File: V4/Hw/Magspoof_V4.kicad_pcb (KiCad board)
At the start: 2 copper layers, 39.5 x 21.9 mm, 47 parts, among them J1 Coil, J2 SWD, P1 USB_C_Plug_USB2.0, Q1 DMG3415U-7, SW1 ON, SW3 S1, SW4 SOURCE MAG, SW5 RESET, U1 CH552G, U2 AP2112K-3.3, U3 TC4424, U5 MCP73831

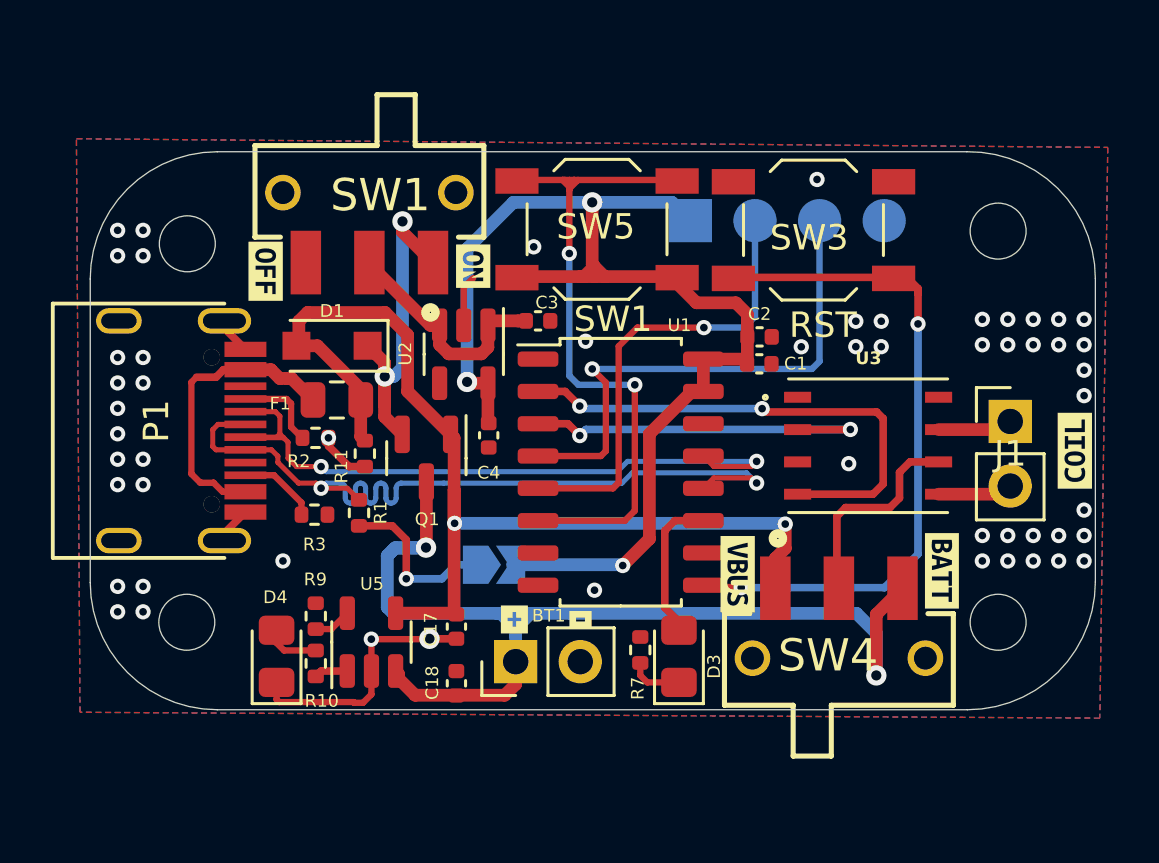
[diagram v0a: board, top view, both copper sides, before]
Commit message: change footprint of SW1,4, and F1 and routing
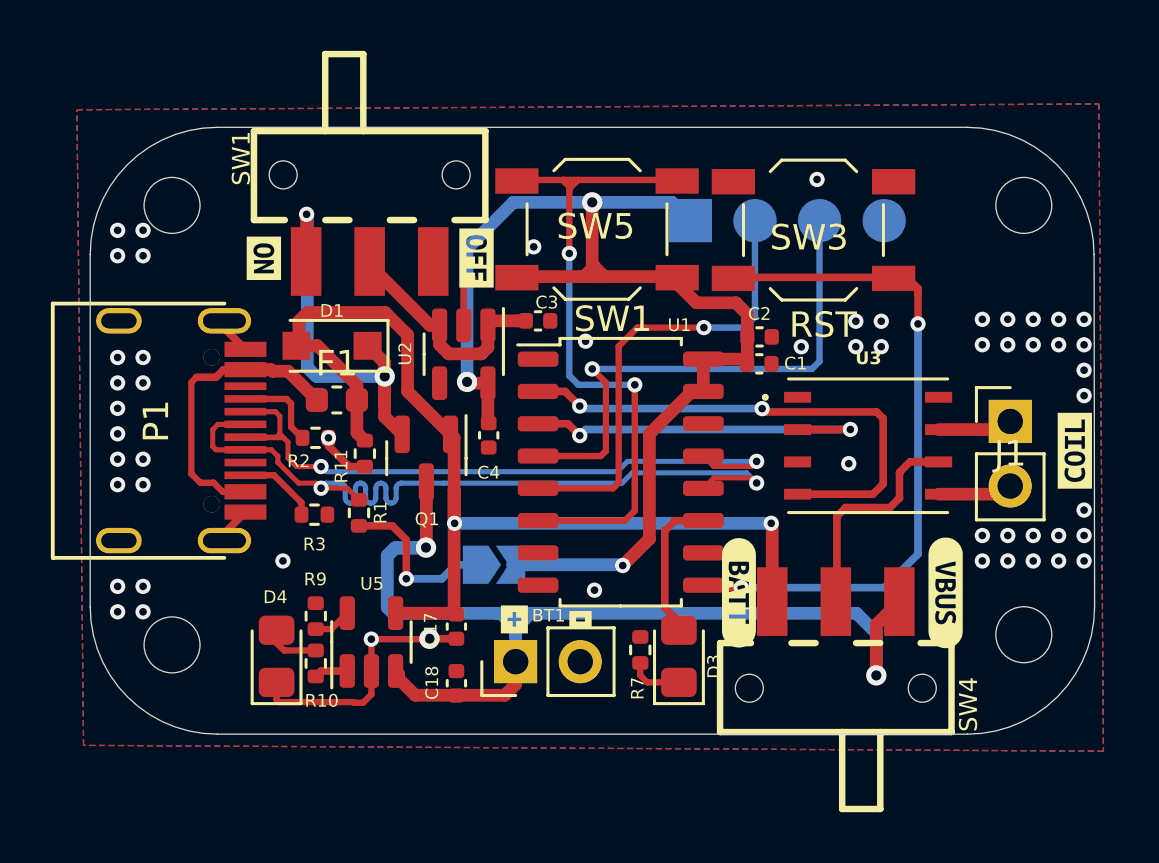
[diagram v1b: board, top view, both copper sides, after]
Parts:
- removed kibuzzard-6436F03D: G***, kibuzzard-6436F03D
- removed kibuzzard-6436F054: G***, kibuzzard-6436F054
- added kibuzzard-64629FC5: G***, kibuzzard-64629FC5, F.Cu at (130.6, 63.8)
- added kibuzzard-64629FDC: G***, kibuzzard-64629FDC, F.Cu at (122.4, 63.8)
- F1: footprint Fuse:Fuse_0805_2012Metric -> Fuse:Fuse_0603_1608Metric
- SW1, SW4: footprint Library:JS102011SAQN -> Library:SW-SMD_K3-1280S-K1
- moved kibuzzard-6436EF98 8.31 mm to (112.1, 50.6)
- moved kibuzzard-6436EF9F 8.24 mm to (103.8, 50.6)
- moved H1 1.62 mm to (100.1, 48.5)
- moved H2 1.43 mm to (133.6, 48.5)
- moved H4 1.12 mm to (133.6, 65.5)
- moved H3 1.06 mm to (100.1, 65.8)
- moved SW1 0.96 mm to (107.9, 50.7), turned to 90 degrees
- moved SW4 0.49 mm to (126.2, 64.1), turned to -90 degrees
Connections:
- SW4 pad 1: VBUS -> +BATT
- SW4 pad 3: +BATT -> VBUS
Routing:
- net Net-(D1-K): track 14.1 -> 16.3 mm
- net Net-(F1-Pad1): track 12.6 -> 11.6 mm
- net +BATT: track 43.3 -> 42.7 mm
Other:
- board size 39.5 x 21.9 mm -> 39.5 x 23.9 mm

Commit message: change SW1 and SW4 for stocks
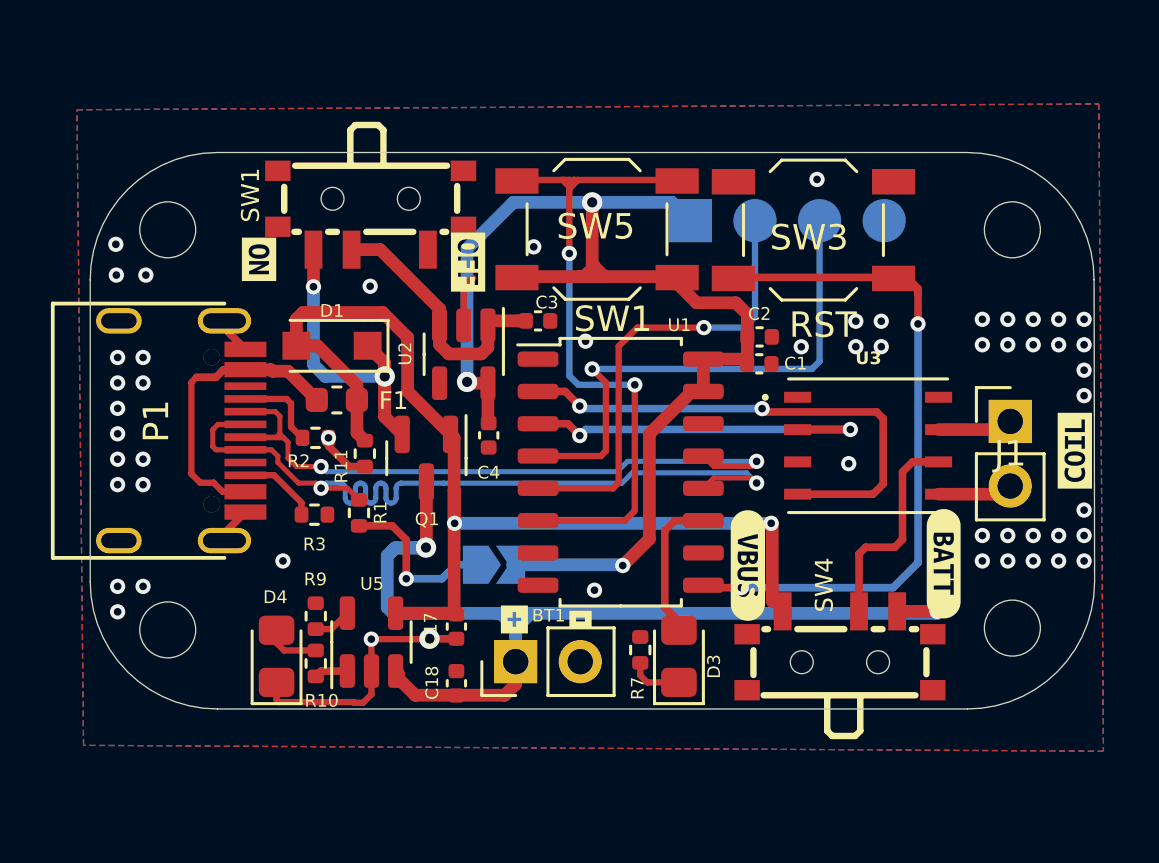
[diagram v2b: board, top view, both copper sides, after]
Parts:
- SW1, SW4: footprint Library:SW-SMD_K3-1280S-K1 -> Library:SW-SMD_SSSS811101
- moved kibuzzard-64629FDC 8.13 mm to (130.5, 62.6)
- moved kibuzzard-64629FC5 7.85 mm to (122.8, 62.7)
- moved SW1 2.02 mm to (108.0, 48.7), turned to 180 degrees
- moved SW4 1.94 mm to (126.4, 66.0), turned to 0 degrees
- moved H2 1.06 mm to (133.2, 49.5)
- moved H1 0.97 mm to (100.0, 49.5)
- moved H3 0.61 mm to (100.0, 65.2)
- moved H4 0.52 mm to (133.2, 65.2)
- moved kibuzzard-6436EF98 0.37 mm to (111.8, 50.8)
- moved kibuzzard-6436EF9F 0.19 mm to (103.6, 50.6)
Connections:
- SW1 pad 1: Net-(D1-K) -> (no net)
- SW1 pad 3: (no net) -> Net-(D1-K)
- SW4 pad 1: +BATT -> VBUS
- SW4 pad 3: VBUS -> +BATT
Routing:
- net Net-(D1-K): track 16.3 -> 12.7 mm
- net +BATT: track 42.7 -> 42.1 mm
- net Net-(SW1-B): track 9.62 -> 10.1 mm
- net GND: vias 55 -> 54
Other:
- board size 39.5 x 23.9 mm -> 39.5 x 21.9 mm

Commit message: Update labels
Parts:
- added REF**: OSHW-Logo_5.7x6mm_SilkScreen, Symbol:OSHW-Logo_5.7x6mm_SilkScreen, B.Cu at (106.2, 57.4)
- added kibuzzard-64665C6A: G***, kibuzzard-64665C6A, F.Cu at (102.5, 66.1)
- added kibuzzard-64665C9F: G***, kibuzzard-64665C9F, B.Cu at (108.7, 62.7)

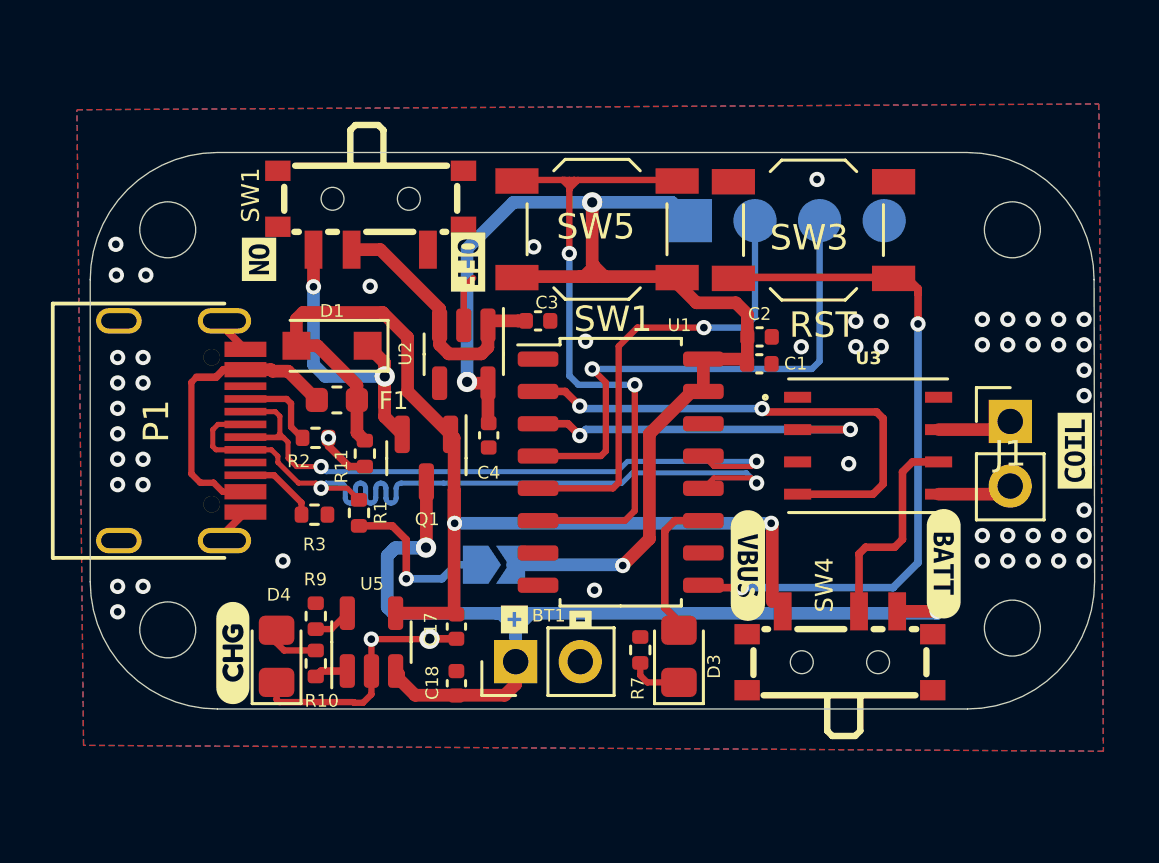
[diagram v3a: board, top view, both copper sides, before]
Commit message: change DFN-8 to SOIC-8 TC4424 and add 3d model of SW1,4
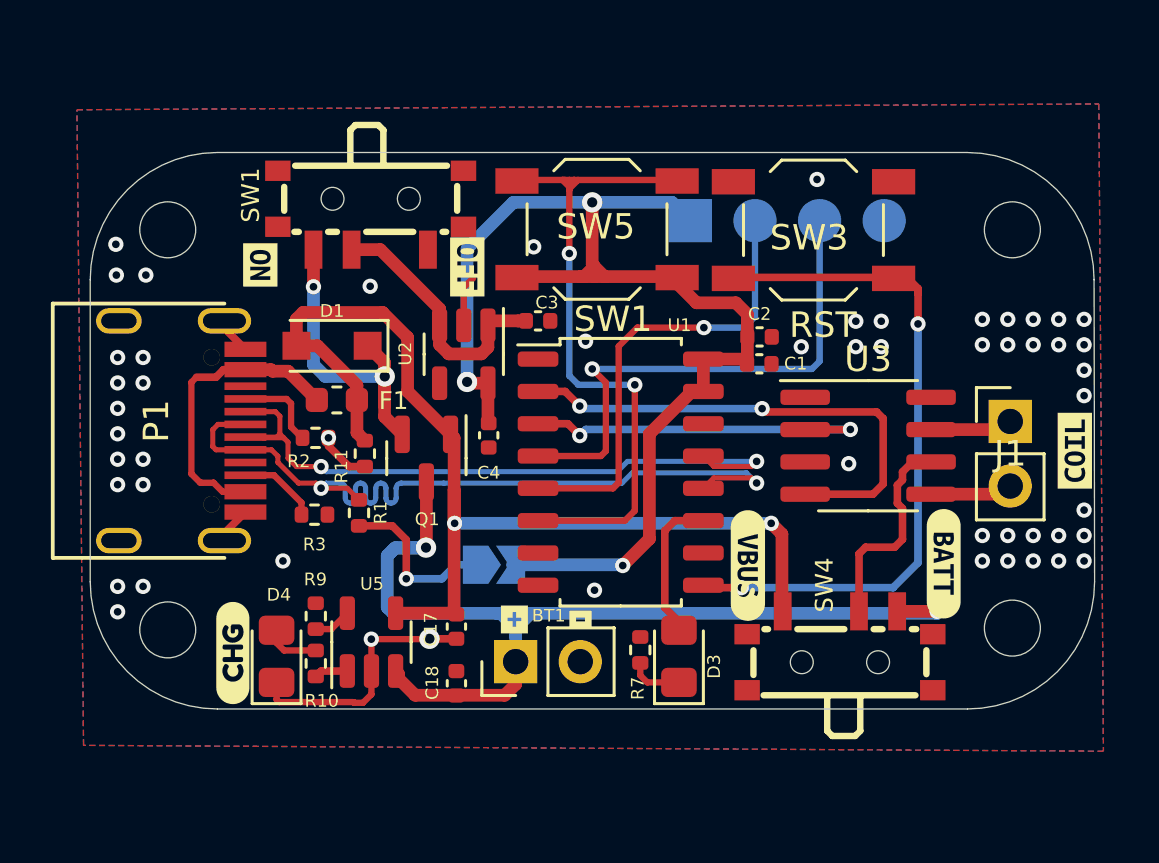
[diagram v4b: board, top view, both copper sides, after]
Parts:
- U3: footprint Library:TC4424EMF(v3) -> Package_SO:SOIC-8_3.9x4.9mm_P1.27mm
- moved kibuzzard-6436EF9F 0.23 mm to (103.6, 50.9)
- moved kibuzzard-6436EF98 0.19 mm to (111.8, 50.9)
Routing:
- net VBUS: track 42.2 -> 42.8 mm

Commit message: fix serigraphy "SW1"for "RST"
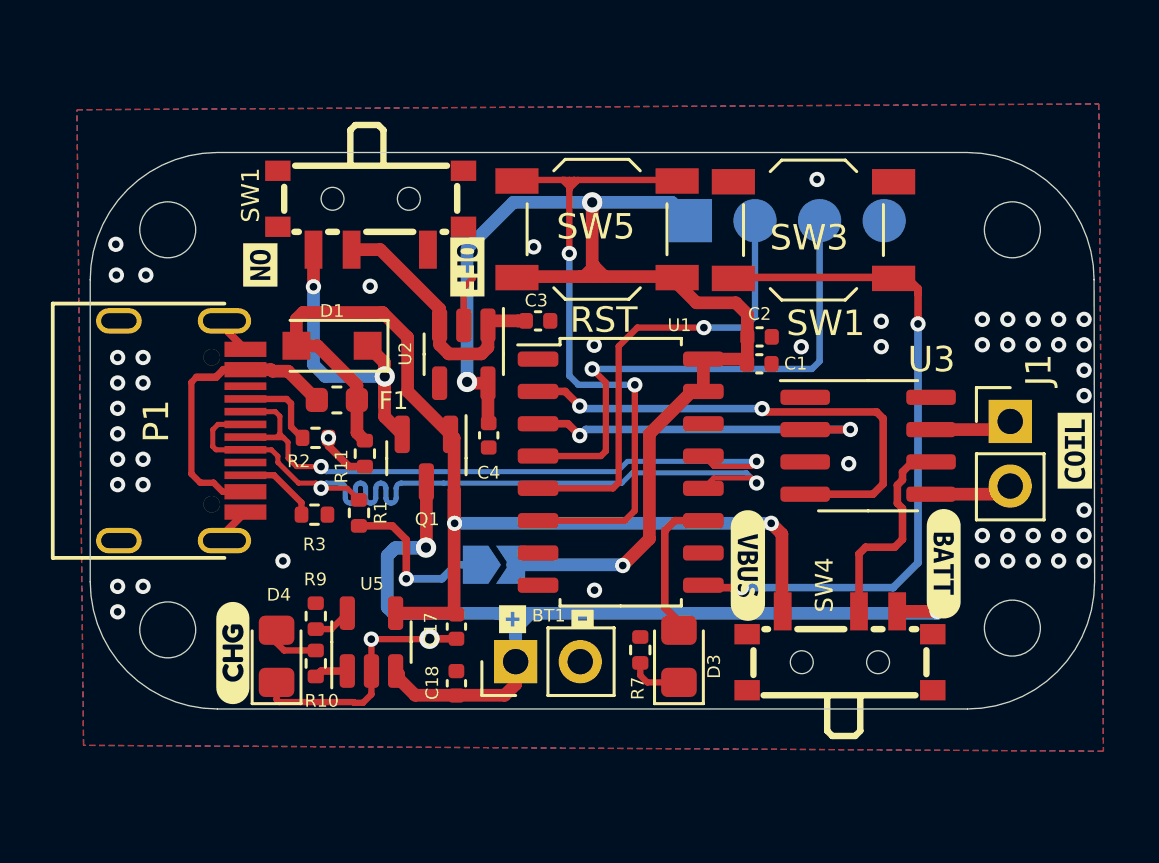
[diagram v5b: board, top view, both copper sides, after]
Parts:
- moved kibuzzard-6436EA46 0.09 mm to (116.3, 64.8)
- moved kibuzzard-6436EA37 0.07 mm to (113.5, 64.8)
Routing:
- net GND: vias 54 -> 52
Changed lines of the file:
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@@
     (property "manf#" "-")
     (attr through_hole)
-    (fp_text reference "J1" (at 0 1.27) (layer "F.SilkS")
+    (fp_text reference "J1" (at 1.124 -2.025 90) (layer "F.SilkS")
         (effects (font (size 1 1) (thickness 0.15)))
     )
@@
     (property "manf#" "TC4424AVOA713")
     (attr smd)
-    (fp_text reference "U3" (at 0 -3.4) (layer "F.SilkS")
+    (fp_text reference "U3" (at 2.492 -3.39) (layer "F.SilkS")
         (effects (font (size 1 1) (thickness 0.15)))
     )
@@
     (property "manf#" "CL05A106MP5NUNC")
     (attr smd)
-    (fp_text reference "C3" (at 0.35 -0.72 180) (layer "F.SilkS")
+    (fp_text reference "C3" (at -0.07 -0.8 180) (layer "F.SilkS")
         (effects (font (size 0.5 0.5) (thickness 0.125)))
     )
@@
   )
   (footprint "kibuzzard-6436EA46" (layer "F.Cu")
-    (at 116.2 64.8)
+    (at 116.28 64.76)
     (descr "Generated with KiBuzzard")
     (tags "kb_params=eyJBbGlnbm1lbnRDaG9pY2UiOiAiQ2VudGVyIiwgIkNhcExlZnRDaG9pY2UiOiAiWyIsICJDYXBSaWdodENob2ljZSI6ICJdIiwgIkZvbnRDb21ib0JveCI6ICJVYnVudHVNb25vLUIiLCAiSGVpZ2h0Q3RybCI6ICIuOCIsICJMYXllckNvbWJvQm94IjogIkYuU2lsa1MiLCAiTXVsdGlMaW5lVGV4dCI6ICItIiwgIlBhZGRpbmdCb3R0b21DdHJsIjogIjUiLCAiUGFkZGluZ0xlZnRDdHJsIjogIjUiLCAiUGFkZGluZ1JpZ2h0Q3RybCI6ICI1IiwgIlBhZGRpbmdUb3BDdHJsIjogIjUiLCAiV2lkdGhDdHJsIjogIiJ9")
@@
   )
   (footprint "kibuzzard-6436EA37" (layer "F.Cu")
-    (at 113.6 64.8)
+    (at 113.53 64.79)
     (descr "Generated with KiBuzzard")
     (tags "kb_params=eyJBbGlnbm1lbnRDaG9pY2UiOiAiQ2VudGVyIiwgIkNhcExlZnRDaG9pY2UiOiAiWyIsICJDYXBSaWdodENob2ljZSI6ICJdIiwgIkZvbnRDb21ib0JveCI6ICJVYnVudHVNb25vLUIiLCAiSGVpZ2h0Q3RybCI6ICIuOCIsICJMYXllckNvbWJvQm94IjogIkYuU2lsa1MiLCAiTXVsdGlMaW5lVGV4dCI6ICIrIiwgIlBhZGRpbmdCb3R0b21DdHJsIjogIjUiLCAiUGFkZGluZ0xlZnRDdHJsIjogIjUiLCAiUGFkZGluZ1JpZ2h0Q3RybCI6ICI1IiwgIlBhZGRpbmdUb3BDdHJsIjogIjUiLCAiV2lkdGhDdHJsIjogIiJ9")
@@
     (effects (font (size 1 1) (thickness 0.15)) (justify mirror))
   )
-  (gr_text "SW1" (at 115.93 53.58) (layer "F.SilkS")
+  (gr_text "SW1" (at 124.29 53.74) (layer "F.SilkS")
     (effects (font (size 1 1) (thickness 0.15)) (justify left bottom))
   )
-  (gr_text "RST" (at 124.4 53.81) (layer "F.SilkS")
+  (gr_text "RST" (at 115.78 53.61) (layer "F.SilkS")
     (effects (font (size 1 1) (thickness 0.15)) (justify left bottom))
   )
@@
   (via (at 128.025 54.075) (size 0.6) (drill 0.3) (layers "F.Cu" "B.Cu") (free) (net 2))
   (via (at 107.975 65.575) (size 0.6) (drill 0.3) (layers "F.Cu" "B.Cu") (net 2))
-  (via (at 116.4 53.86) (size 0.6) (drill 0.3) (layers "F.Cu" "B.Cu") (free) (net 2))
+  (via (at 116.74 54.02) (size 0.6) (drill 0.3) (layers "F.Cu" "B.Cu") (free) (net 2))
   (via (at 107.93 51.7) (size 0.6) (drill 0.3) (layers "F.Cu" "B.Cu") (free) (net 2))
   (via (at 126.746 58.674) (size 0.6) (drill 0.3) (layers "F.Cu" "B.Cu") (free) (net 2))
@@
   (via (at 110.26 65.56) (size 0.8) (drill 0.4) (layers "F.Cu" "B.Cu") (net 2))
   (via (at 132 61.5) (size 0.6) (drill 0.3) (layers "F.Cu" "B.Cu") (free) (net 2))
-  (via (at 127.025 54.075) (size 0.6) (drill 0.3) (layers "F.Cu" "B.Cu") (free) (net 2))
   (via (at 99 63.5) (size 0.6) (drill 0.3) (layers "F.Cu" "B.Cu") (free) (net 2))
   (via (at 98 55.5) (size 0.6) (drill 0.3) (layers "F.Cu" "B.Cu") (free) (net 2))
@@
   (via (at 98 63.5) (size 0.6) (drill 0.3) (layers "F.Cu" "B.Cu") (free) (net 2))
   (via (at 134 53) (size 0.6) (drill 0.3) (layers "F.Cu" "B.Cu") (free) (net 2))
-  (via (at 127.025 53.075) (size 0.6) (drill 0.3) (layers "F.Cu" "B.Cu") (free) (net 2))
   (via (at 132 53) (size 0.6) (drill 0.3) (layers "F.Cu" "B.Cu") (free) (net 2))
   (segment (start 116.2 51.32) (end 116.34 51.32) (width 0.5) (layer "F.Cu") (net 3))
